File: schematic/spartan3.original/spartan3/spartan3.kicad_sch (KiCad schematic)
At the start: 65 parts

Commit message: 1.CPU control & Clock blocks added. 2.Slider switch library added.
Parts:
- added D_in_clk_manual_0, D_in_is_clk_external_0, D_in_is_clk_high_0, D_in_is_clk_low_0, D_in_is_clk_manual_0, D_in_is_clk_veryhigh_0, D_out_acc_r_0, D_out_acc_w_0, D_out_bus1_0, D_out_flags_w_0, D_out_iar_r_0, D_out_iar_w_0, D_out_ir_w_0, D_out_r0_r_0, D_out_r0_w_0, D_out_r1_r_0, D_out_r1_w_0, D_out_r2_r_0, D_out_r2_w_0, D_out_r3_r_0, D_out_r3_w_0, D_out_ram_a_w_0, D_out_ram_r_0, D_out_ram_w_0, D_out_temp_w_0: LED_Small, symbol Device:LED_Small
- added R_in_clk_manual_0, R_in_is_clk_external_0, R_in_is_clk_high_0, R_in_is_clk_low_0, R_in_is_clk_manual_0, R_in_is_clk_veryhigh_0: 1K, symbol Device:R_US
- added R_out_acc_r_0, R_out_acc_w_0, R_out_bus1_0, R_out_flags_w_0, R_out_iar_r_0, R_out_iar_w_0, R_out_ir_w_0, R_out_r0_r_0, R_out_r0_w_0, R_out_r1_r_0, R_out_r1_w_0, R_out_r2_r_0, R_out_r2_w_0, R_out_r3_r_0, R_out_r3_w_0, R_out_ram_a_w_0, R_out_ram_r_0, R_out_ram_w_0, R_out_temp_w_0: 100R, symbol Device:R_US
- added SW_in_clk_manual_0: SW_Push, symbol Switch:SW_Push
- added U?: SPFT_Sliding_Switch-dynacore, symbol sliders:SPFT_Sliding_Switch-dynacore
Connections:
- net GND: now also SW_in_manual_input_o_0.1 (A), SW_in_manual_input_o_1.1 (A), SW_in_manual_input_o_2.1 (A), SW_in_manual_input_o_3.1 (A), SW_in_manual_input_o_4.1 (A), SW_in_manual_input_o_5.1 (A), SW_in_manual_input_o_6.1 (A), SW_in_manual_input_o_7.1 (A), R_out_acc_r_0.2, R_out_acc_w_0.2, R_out_bus1_0.2, R_out_flags_w_0.2, R_out_iar_r_0.2, R_out_iar_w_0.2, R_out_ir_w_0.2, R_out_r0_r_0.2, R_out_r0_w_0.2, R_out_r1_r_0.2, R_out_r1_w_0.2, R_out_r2_r_0.2, R_out_r2_w_0.2, R_out_r3_r_0.2, R_out_r3_w_0.2, R_out_ram_a_w_0.2, R_out_ram_r_0.2, R_out_ram_w_0.2, R_out_temp_w_0.2, SW_in_clk_manual_0.2, U?.~ (P5); no longer R_in_manual_input_o_0.2, R_in_manual_input_o_1.2, R_in_manual_input_o_2.2, R_in_manual_input_o_3.2, R_in_manual_input_o_4.2, R_in_manual_input_o_5.2, R_in_manual_input_o_6.2, R_in_manual_input_o_7.2
- net VCC: now also R_in_manual_input_o_0.2, R_in_manual_input_o_1.2, R_in_manual_input_o_2.2, R_in_manual_input_o_3.2, R_in_manual_input_o_4.2, R_in_manual_input_o_5.2, R_in_manual_input_o_6.2, R_in_manual_input_o_7.2, D_in_clk_manual_0.2 (A), D_in_is_clk_external_0.2 (A), D_in_is_clk_high_0.2 (A), D_in_is_clk_low_0.2 (A), D_in_is_clk_manual_0.2 (A), D_in_is_clk_veryhigh_0.2 (A), R_in_clk_manual_0.2, R_in_is_clk_external_0.2, R_in_is_clk_high_0.2, R_in_is_clk_low_0.2, R_in_is_clk_manual_0.2, R_in_is_clk_veryhigh_0.2; no longer SW_in_manual_input_o_0.1 (A), SW_in_manual_input_o_1.1 (A), SW_in_manual_input_o_2.1 (A), SW_in_manual_input_o_3.1 (A), SW_in_manual_input_o_4.1 (A), SW_in_manual_input_o_5.1 (A), SW_in_manual_input_o_6.1 (A), SW_in_manual_input_o_7.1 (A)
- new net: D_out_r3_w_0.2 (A), R_out_r3_w_0.1
- new net: D_out_r3_r_0.2 (A), R_out_r3_r_0.1
- new net: D_out_temp_w_0.2 (A), R_out_temp_w_0.1
- new net: D_out_iar_r_0.2 (A), R_out_iar_r_0.1
- new net: D_out_r1_r_0.2 (A), R_out_r1_r_0.1
- new net: D_out_ir_w_0.2 (A), R_out_ir_w_0.1
- new net: D_out_r0_w_0.2 (A), R_out_r0_w_0.1
- new net: D_out_r2_r_0.2 (A), R_out_r2_r_0.1
- new net: D_out_ram_a_w_0.2 (A), R_out_ram_a_w_0.1
- new net: D_out_r2_w_0.2 (A), R_out_r2_w_0.1
- new net: D_out_iar_w_0.2 (A), R_out_iar_w_0.1
- new net: D_out_ram_w_0.2 (A), R_out_ram_w_0.1
- new net: D_out_acc_w_0.2 (A), R_out_acc_w_0.1
- new net: D_out_ram_r_0.2 (A), R_out_ram_r_0.1
- new net: D_out_flags_w_0.2 (A), R_out_flags_w_0.1
- new net: D_out_r1_w_0.2 (A), R_out_r1_w_0.1
- new net: D_out_r0_r_0.2 (A), R_out_r0_r_0.1
- new net: D_out_acc_r_0.2 (A), R_out_acc_r_0.1
- new net: D_out_bus1_0.2 (A), R_out_bus1_0.1
- new net in_clk_manual: D_in_clk_manual_0.1 (K), R_in_clk_manual_0.1, SW_in_clk_manual_0.1
- new net in_is_clk_external: D_in_is_clk_external_0.1 (K), R_in_is_clk_external_0.1, U?.~ (P5)
- new net in_is_clk_high: D_in_is_clk_high_0.1 (K), R_in_is_clk_high_0.1, U?.~ (P5)
- new net in_is_clk_low: D_in_is_clk_low_0.1 (K), R_in_is_clk_low_0.1, U?.~ (P5)
- new net in_is_clk_manual: D_in_is_clk_manual_0.1 (K), R_in_is_clk_manual_0.1, U?.~ (P5)
- new net in_is_clk_veryhigh: D_in_is_clk_veryhigh_0.1 (K), R_in_is_clk_veryhigh_0.1, U?.~ (P5)
- new net out_acc_r: D_out_acc_r_0.1 (K)
- new net out_acc_w: D_out_acc_w_0.1 (K)
- new net out_bus1: D_out_bus1_0.1 (K)
- new net out_flags_w: D_out_flags_w_0.1 (K)
- new net out_iar_r: D_out_iar_r_0.1 (K)
- new net out_iar_w: D_out_iar_w_0.1 (K)
- new net out_ir_w: D_out_ir_w_0.1 (K)
- new net out_r0_r: D_out_r0_r_0.1 (K)
- new net out_r0_w: D_out_r0_w_0.1 (K)
- new net out_r1_r: D_out_r1_r_0.1 (K)
- new net out_r1_w: D_out_r1_w_0.1 (K)
- new net out_r2_r: D_out_r2_r_0.1 (K)
- new net out_r2_w: D_out_r2_w_0.1 (K)
- new net out_r3_r: D_out_r3_r_0.1 (K)
- new net out_r3_w: D_out_r3_w_0.1 (K)
- new net out_ram_a_w: D_out_ram_a_w_0.1 (K)
- new net out_ram_r: D_out_ram_r_0.1 (K)
- new net out_ram_w: D_out_ram_w_0.1 (K)
- new net out_temp_w: D_out_temp_w_0.1 (K)
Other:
- note added: "Clock"
- note added: "TODO: Check connections"
- moved on the sheet: D_out_clk_internal_0, R_out_clk_internal_0

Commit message: Schematics :: Read Register block added
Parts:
- added D_in_acc_r_0, D_in_iar_r_0, D_in_ir_r_0, D_in_manual_input_r_0, D_in_r0_r_0, D_in_r1_r_0, D_in_r2_r_0, D_in_r3_r_0, D_in_ram_r_0, D_in_read_reg_en_0, D_out_can_read_0: LED_Small, symbol Device:LED_Small
- added R_in_acc_r_0, R_in_iar_r_0, R_in_ir_r_0, R_in_manual_input_r_0, R_in_r0_r_0, R_in_r1_r_0, R_in_r2_r_0, R_in_r3_r_0, R_in_ram_r_0, R_in_read_reg_en_0: 1K, symbol Device:R_US
- added R_out_can_read_0: 100R, symbol Device:R_US
- added SW_in_read_reg_en_0: SW_Push, symbol Switch:SW_Push
- added SW_read_register_0: SW_Rotary12, symbol Switch:SW_Rotary12
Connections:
- net GND: now also R_out_can_read_0.2, SW_in_read_reg_en_0.2, SW_read_register_0.13
- net VCC: now also D_in_acc_r_0.2 (A), D_in_iar_r_0.2 (A), D_in_ir_r_0.2 (A), D_in_manual_input_r_0.2 (A), D_in_r0_r_0.2 (A), D_in_r1_r_0.2 (A), D_in_r2_r_0.2 (A), D_in_r3_r_0.2 (A), D_in_ram_r_0.2 (A), D_in_read_reg_en_0.2 (A), R_in_acc_r_0.2, R_in_iar_r_0.2, R_in_ir_r_0.2, R_in_manual_input_r_0.2, R_in_r0_r_0.2, R_in_r1_r_0.2, R_in_r2_r_0.2, R_in_r3_r_0.2, R_in_ram_r_0.2, R_in_read_reg_en_0.2
- new net: D_out_can_read_0.2 (A), R_out_can_read_0.1
- new net in_acc_r: D_in_acc_r_0.1 (K), R_in_acc_r_0.1, SW_read_register_0.3
- new net in_iar_r: D_in_iar_r_0.1 (K), R_in_iar_r_0.1, SW_read_register_0.1
- new net in_ir_r: D_in_ir_r_0.1 (K), R_in_ir_r_0.1, SW_read_register_0.2
- new net in_manual_input_r: D_in_manual_input_r_0.1 (K), R_in_manual_input_r_0.1, SW_read_register_0.9
- new net in_r0_r: D_in_r0_r_0.1 (K), R_in_r0_r_0.1, SW_read_register_0.5
- new net in_r1_r: D_in_r1_r_0.1 (K), R_in_r1_r_0.1, SW_read_register_0.6
- new net in_r2_r: D_in_r2_r_0.1 (K), R_in_r2_r_0.1, SW_read_register_0.7
- new net in_r3_r: D_in_r3_r_0.1 (K), R_in_r3_r_0.1, SW_read_register_0.8
- new net in_ram_r: D_in_ram_r_0.1 (K), R_in_ram_r_0.1, SW_read_register_0.4
- new net in_read_reg_en: D_in_read_reg_en_0.1 (K), R_in_read_reg_en_0.1, SW_in_read_reg_en_0.1
- new net out_can_read: D_out_can_read_0.1 (K)
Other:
- note added: "Read Register"
- note added: "TODO: check connections"
- moved on the sheet: U?A, U?B, U?C

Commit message: Schematics :: 1.Write Register added 2.1/PS Bus added
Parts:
- removed SW_in_read_reg_en_0: SW_Push, symbol Switch:SW_Push
- added D_in_acc_w_0, D_in_bus1_one_0, D_in_bus1_ps_0, D_in_iar_w_0, D_in_ir_w_0, D_in_is_bus1_w_0, D_in_r0_w_0, D_in_r1_w_0, D_in_r2_w_0, D_in_r3_w_0, D_in_ram_a_w_0, D_in_ram_w_0, D_in_temp_w_0, D_in_write_reg_en_0, D_out_can_write_0, D_out_is_bus1_w_0: LED_Small, symbol Device:LED_Small
- added R_in_acc_w_0, R_in_bus1_0, R_in_iar_w_0, R_in_ir_w_0, R_in_is_bus1_w_0, R_in_r0_w_0, R_in_r1_w_0, R_in_r2_w_0, R_in_r3_w_0, R_in_ram_a_w_0, R_in_ram_w_0, R_in_temp_w_0, R_in_write_reg_en_0: 1K, symbol Device:R_US
- added R_out_can_write_0, R_out_is_bus1_w_0: 100R, symbol Device:R_US
- added SW_in_acc_w_0, SW_in_bus1_0, SW_in_iar_w_0, SW_in_ir_w_0, SW_in_is_bus1_w_0, SW_in_r0_w_0, SW_in_r1_w_0, SW_in_r2_w_0, SW_in_r3_w_0, SW_in_ram_a_w_0, SW_in_ram_w_0, SW_in_read_reg_en_0, SW_in_temp_w_0, SW_in_write_reg_en_0: SW_DPDT_x2, symbol Switch:SW_DPDT_x2
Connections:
- net GND: now also D_in_bus1_ps_0.1 (K), R_out_can_write_0.2, R_out_is_bus1_w_0.2, SW_in_acc_w_0.1 (A), SW_in_bus1_0.1 (A), SW_in_iar_w_0.1 (A), SW_in_ir_w_0.1 (A), SW_in_is_bus1_w_0.1 (A), SW_in_r0_w_0.1 (A), SW_in_r1_w_0.1 (A), SW_in_r2_w_0.1 (A), SW_in_r3_w_0.1 (A), SW_in_ram_a_w_0.1 (A), SW_in_ram_w_0.1 (A), SW_in_read_reg_en_0.1 (A), SW_in_temp_w_0.1 (A), SW_in_write_reg_en_0.1 (A)
- net VCC: now also D_in_acc_w_0.2 (A), D_in_bus1_one_0.1 (K), D_in_iar_w_0.2 (A), D_in_ir_w_0.2 (A), D_in_is_bus1_w_0.2 (A), D_in_r0_w_0.2 (A), D_in_r1_w_0.2 (A), D_in_r2_w_0.2 (A), D_in_r3_w_0.2 (A), D_in_ram_a_w_0.2 (A), D_in_ram_w_0.2 (A), D_in_temp_w_0.2 (A), D_in_write_reg_en_0.2 (A), R_in_acc_w_0.2, R_in_bus1_0.2, R_in_iar_w_0.2, R_in_ir_w_0.2, R_in_is_bus1_w_0.2, R_in_r0_w_0.2, R_in_r1_w_0.2, R_in_r2_w_0.2, R_in_r3_w_0.2, R_in_ram_a_w_0.2, R_in_ram_w_0.2, R_in_temp_w_0.2, R_in_write_reg_en_0.2, SW_in_bus1_0.3 (C)
- net in_read_reg_en: now also SW_in_read_reg_en_0.2 (B)
- new net: D_out_is_bus1_w_0.2 (A), R_out_is_bus1_w_0.1
- new net: D_out_can_write_0.2 (A), R_out_can_write_0.1
- new net in_acc_w: D_in_acc_w_0.1 (K), R_in_acc_w_0.1, SW_in_acc_w_0.2 (B)
- new net in_bus1: D_in_bus1_one_0.2 (A), D_in_bus1_ps_0.2 (A), R_in_bus1_0.1, SW_in_bus1_0.2 (B)
- new net in_iar_w: D_in_iar_w_0.1 (K), R_in_iar_w_0.1, SW_in_iar_w_0.2 (B)
- new net in_ir_w: D_in_ir_w_0.1 (K), R_in_ir_w_0.1, SW_in_ir_w_0.2 (B)
- new net in_is_bus1_w: D_in_is_bus1_w_0.1 (K), R_in_is_bus1_w_0.1, SW_in_is_bus1_w_0.2 (B)
- new net in_r0_w: D_in_r0_w_0.1 (K), R_in_r0_w_0.1, SW_in_r0_w_0.2 (B)
- new net in_r1_w: D_in_r1_w_0.1 (K), R_in_r1_w_0.1, SW_in_r1_w_0.2 (B)
- new net in_r2_w: D_in_r2_w_0.1 (K), R_in_r2_w_0.1, SW_in_r2_w_0.2 (B)
- new net in_r3_w: D_in_r3_w_0.1 (K), R_in_r3_w_0.1, SW_in_r3_w_0.2 (B)
- new net in_ram_a_w: D_in_ram_a_w_0.1 (K), R_in_ram_a_w_0.1, SW_in_ram_a_w_0.2 (B)
- new net in_ram_w: D_in_ram_w_0.1 (K), R_in_ram_w_0.1, SW_in_ram_w_0.2 (B)
- new net in_temp_w: D_in_temp_w_0.1 (K), R_in_temp_w_0.1, SW_in_temp_w_0.2 (B)
- new net in_write_reg_en: D_in_write_reg_en_0.1 (K), R_in_write_reg_en_0.1, SW_in_write_reg_en_0.2 (B)
- new net out_can_write: D_out_can_write_0.1 (K)
- new net out_is_bus1_w: D_out_is_bus1_w_0.1 (K)
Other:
- note added: "1/Passthrough"
- note added: "Write Register"
- moved on the sheet: U?A, U?B, U?C

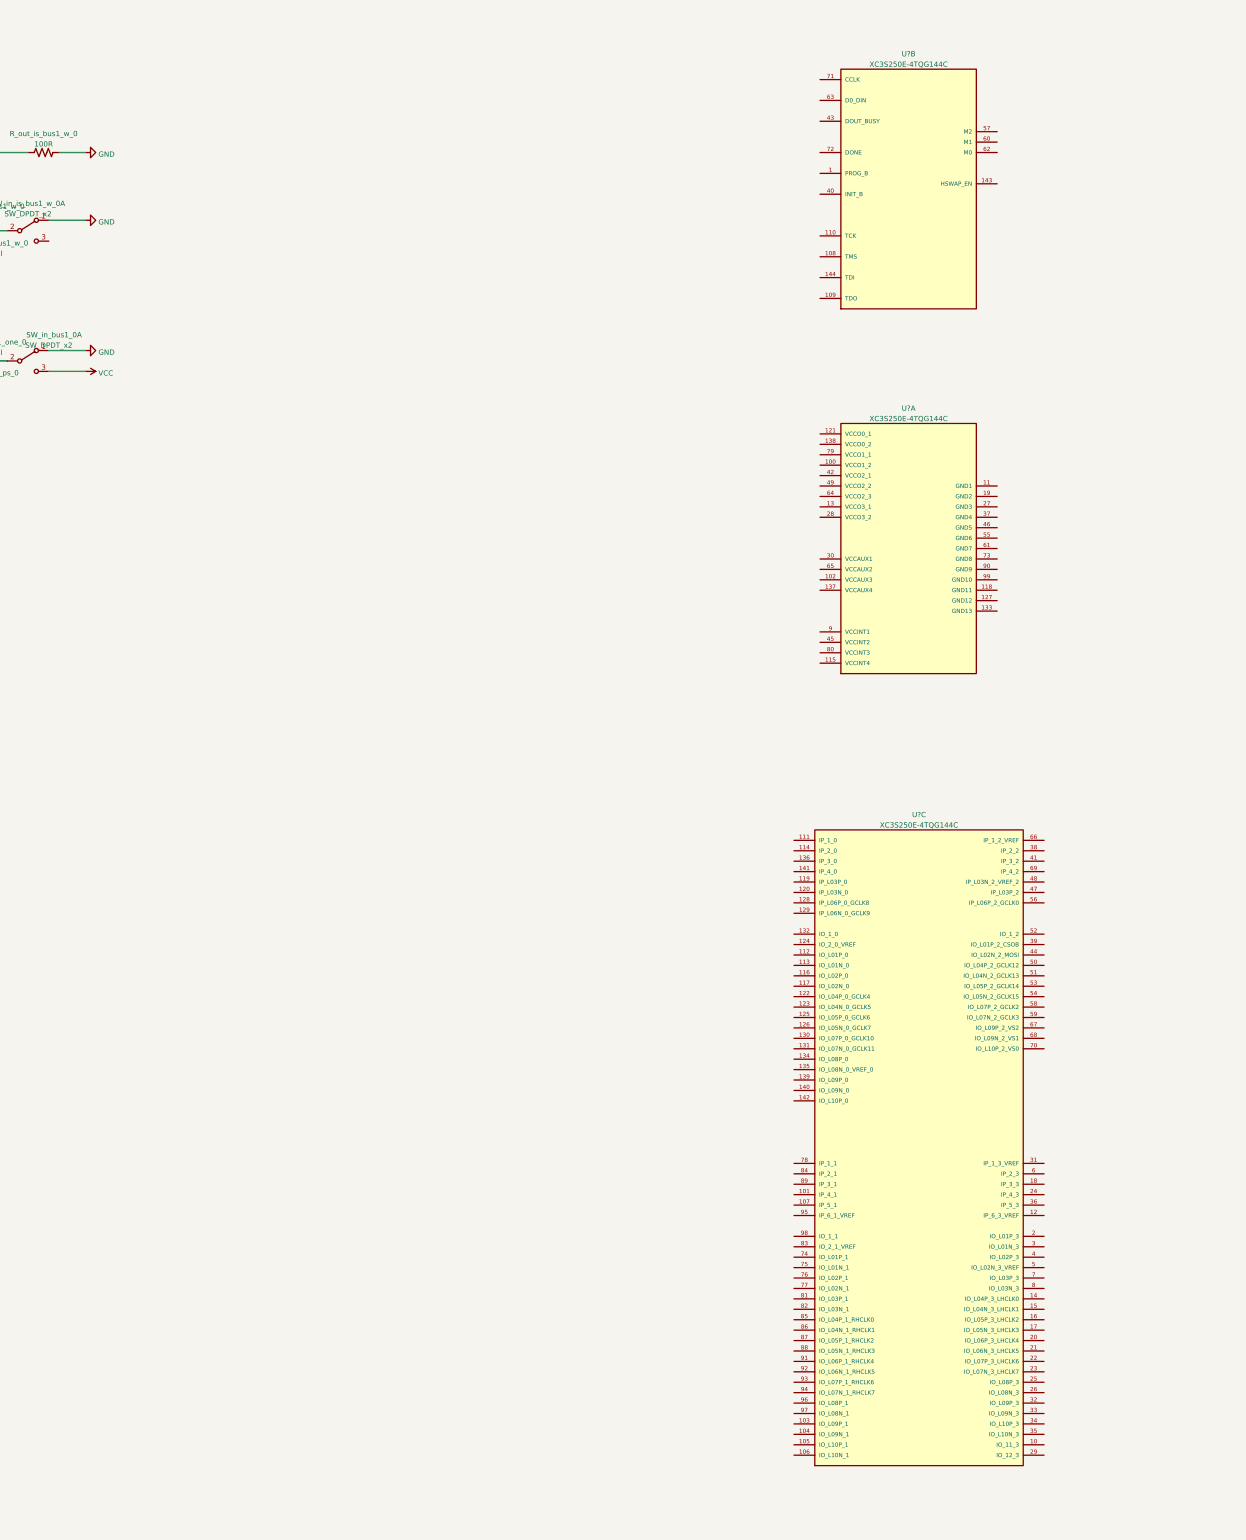
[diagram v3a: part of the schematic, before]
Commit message: Schematic :: Power/Clock/JTAG/EEPROM schematics added
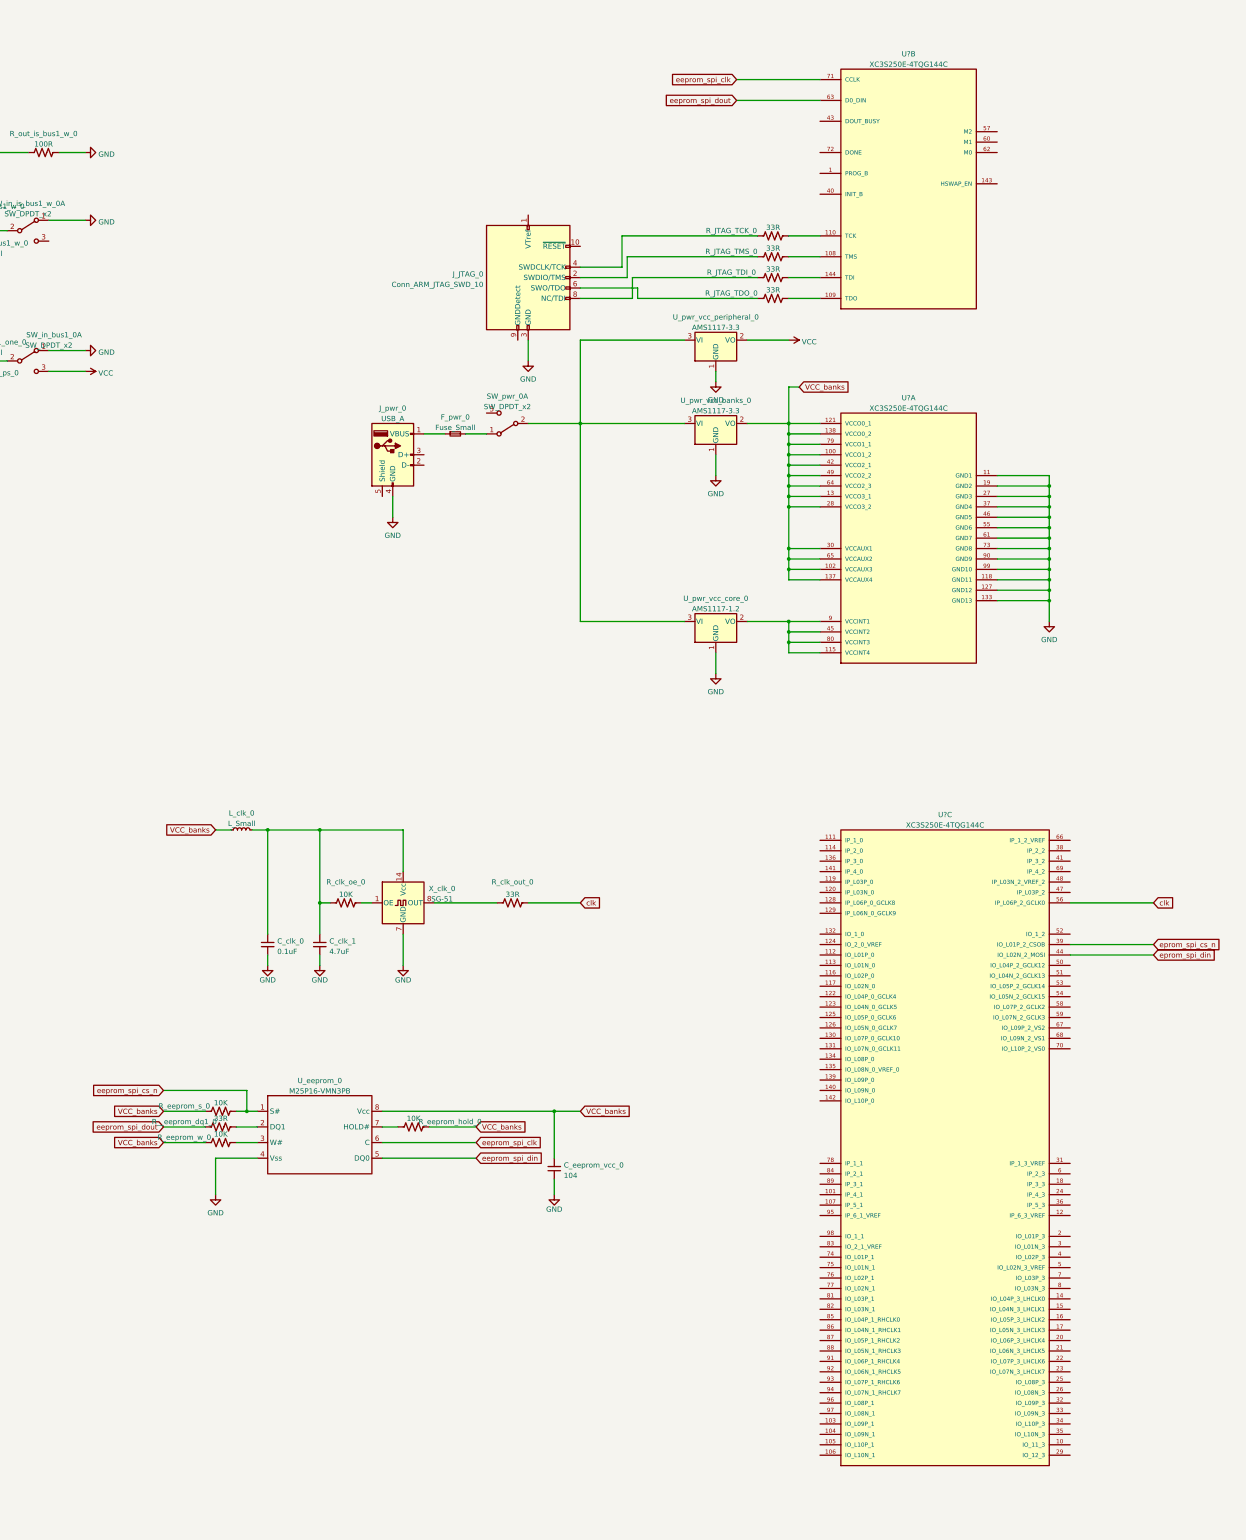
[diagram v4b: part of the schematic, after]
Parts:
- added C_clk_0: 0.1uF, symbol Device:C_Small
- added C_clk_1: 4.7uF, symbol Device:C_Small
- added C_eeprom_vcc_0: 104, symbol Device:C_Small
- added F_pwr_0: Fuse_Small, symbol Device:Fuse_Small
- added J_JTAG_0: Conn_ARM_JTAG_SWD_10, symbol Connector:Conn_ARM_JTAG_SWD_10
- added J_pwr_0: USB_A, symbol Connector:USB_A
- added L_clk_0: L_Small, symbol Device:L_Small
- added R_JTAG_TCK_0, R_JTAG_TDI_0, R_JTAG_TDO_0, R_JTAG_TMS_0, R__eeprom_dq1_0, R_clk_out_0: 33R, symbol Device:R_US
- added R_clk_oe_0, R_eeprom_hold_0, R_eeprom_s_0, R_eeprom_w_0: 10K, symbol Device:R_US
- added SW_pwr_0: SW_DPDT_x2, symbol Switch:SW_DPDT_x2
- added U_eeprom_0: M25P16-VMN3PB, symbol sliders:M25P16-VMN3PB
- added U_pwr_vcc_banks_0, U_pwr_vcc_peripheral_0: AMS1117-3.3, Package_TO_SOT_SMD:SOT-223-3_TabPin2, symbol Regulator_Linear:AMS1117-3.3
- added U_pwr_vcc_core_0: AMS1117-1.2, Package_TO_SOT_SMD:SOT-223-3_TabPin2, symbol Regulator_Linear:AMS1117-1.5
- added X_clk_0: SG-51, Oscillator:Oscillator_SeikoEpson_SG-8002DB, symbol Oscillator:SG-51
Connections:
- net GND: now also U?.11 (GND1), U?.118 (GND11), U?.127 (GND12), U?.133 (GND13), U?.19 (GND2), U?.27 (GND3), U?.37 (GND4), U?.46 (GND5), U?.55 (GND6), U?.61 (GND7), U?.73 (GND8), U?.90 (GND9), U?.99 (GND10), C_clk_0.2, C_clk_1.2, C_eeprom_vcc_0.1, J_JTAG_0.3 (GND), J_JTAG_0.5 (GND), J_pwr_0.4 (GND), U_eeprom_0.4 (Vss), U_pwr_vcc_banks_0.1 (GND), U_pwr_vcc_core_0.1 (GND), U_pwr_vcc_peripheral_0.1 (GND), X_clk_0.7 (GND)
- net VCC: now also U_pwr_vcc_peripheral_0.2 (VO)
- net eprom_spi_cs_n: now reaches U?.39 (IO_L01P_2_CSOB)
- net eprom_spi_din: now reaches U?.44 (IO_L02N_2_MOSI)
- net clk: now reaches U?.56 (IP_L06P_2_GCLK0)
- net clk: now also R_clk_out_0.2
- net VCC_banks: now reaches U?.100 (VCCO1_2)
- net VCC_banks: now also U?.102 (VCCAUX3), U?.121 (VCCO0_1), U?.13 (VCCO3_1), U?.137 (VCCAUX4), U?.138 (VCCO0_2), U?.28 (VCCO3_2), U?.30 (VCCAUX1), U?.42 (VCCO2_1), U?.49 (VCCO2_2), U?.64 (VCCO2_3), U?.65 (VCCAUX2), U?.79 (VCCO1_1), C_eeprom_vcc_0.2, L_clk_0.1, R_eeprom_hold_0.2, R_eeprom_s_0.1, R_eeprom_w_0.1, U_eeprom_0.8 (Vcc), U_pwr_vcc_banks_0.2 (VO)
- net at U?.115 (VCCINT4): now also U?.45 (VCCINT2), U?.80 (VCCINT3), U?.9 (VCCINT1), U_pwr_vcc_core_0.2 (VO)
- net at U?.108 (TMS): now also R_JTAG_TMS_0.2
- net at U?.109 (TDO): now also R_JTAG_TDO_0.2
- net at U?.110 (TCK): now also R_JTAG_TCK_0.2
- net at U?.144 (TDI): now also R_JTAG_TDI_0.2
- net eeprom_spi_dout: now reaches U?.63 (D0_DIN)
- net eeprom_spi_dout: now also R__eeprom_dq1_0.1
- net eeprom_spi_clk: now reaches U?.71 (CCLK)
- net eeprom_spi_clk: now also U_eeprom_0.6 (C)
- new net: R__eeprom_dq1_0.2, U_eeprom_0.2 (DQ1)
- new net: F_pwr_0.1, J_pwr_0.1 (VBUS)
- new net: J_JTAG_0.4 (SWDCLK/TCK), R_JTAG_TCK_0.1
- new net: C_clk_0.1, C_clk_1.1, L_clk_0.2, R_clk_oe_0.1, X_clk_0.14 (Vcc)
- new net: J_JTAG_0.2 (SWDIO/TMS), R_JTAG_TMS_0.1
- new net: J_JTAG_0.6 (SWO/TDO), R_JTAG_TDO_0.1
- new net: J_JTAG_0.8 (NC/TDI), R_JTAG_TDI_0.1
- new net: SW_pwr_0.2 (B), U_pwr_vcc_banks_0.3 (VI), U_pwr_vcc_core_0.3 (VI), U_pwr_vcc_peripheral_0.3 (VI)
- new net: R_eeprom_w_0.2, U_eeprom_0.3 (W#)
- new net: R_eeprom_hold_0.1, U_eeprom_0.7 (HOLD#)
- new net: R_clk_out_0.1, X_clk_0.8 (OUT)
- new net: R_clk_oe_0.2, X_clk_0.1 (OE)
- new net: F_pwr_0.2, SW_pwr_0.1 (A)
- new net eeprom_spi_cs_n: R_eeprom_s_0.2, U_eeprom_0.1 (S#)
- new net eeprom_spi_din: U_eeprom_0.5 (DQ0)
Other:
- moved on the sheet: U?A, U?C
